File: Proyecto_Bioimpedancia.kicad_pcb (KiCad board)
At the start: 2 copper layers, 99.9 x 99.8 mm, 67 parts, among them J1 Jumper, J2 Jumper, J3 Jumper_Calibration, J4 Jumper, J5 Jumper, J6 Jumper, P1 CONN_01X05, P10 CONN_01X03, P11 CONN_01X02, P12 CONN_01X01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

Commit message: PCB-1_Prototipo_1
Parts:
- removed C14: 10uF, Capacitors_SMD:C_0805_HandSoldering
- removed P17: CONN_01X02, Socket_Strips:Socket_Strip_Straight_1x02_Pitch2.54mm
- added D3: Z_PROTEC, Diodes_THT:D_DO-41_SOD81_P10.16mm_Horizontal, F.Cu at (141.2, 70.6)
- added D4: Z_PROTEC, Diodes_THT:D_DO-41_SOD81_P10.16mm_Horizontal, F.Cu at (136.8, 65.0)
- added R17: 10K, Resistors_SMD:R_0805_HandSoldering, F.Cu at (133.9, 63.6)
- added W6: TEST_1P, Measurement_Points:Measurement_Point_Round-TH_Small, F.Cu at (100.4, 104.7)
- C10: value 1uF -> 0,1uF
- C11: value 1uF -> 10uF
- C13: value 1nF -> 10uF; footprint Capacitors_SMD:C_1206_HandSoldering -> Capacitors_SMD:C_0805_HandSoldering
- P1: value CONN_01X05 -> PROTECCION_MICRO; footprint Socket_Strips:Socket_Strip_Straight_1x05_Pitch2.54mm -> Sockets_MOLEX_KK-System:Socket_MOLEX-KK-RM3-96mm_Lock_3pin_straight
- P10: value CONN_01X03 -> RS-232
- P11: value CONN_01X02 -> SOURCE_2; footprint Socket_Strips:Socket_Strip_Straight_1x02_Pitch2.54mm -> Sockets_MOLEX_KK-System:Socket_MOLEX-KK-RM3-96mm_Lock_2pin_straight
- P12: value CONN_01X01 -> RESET
- P13: value CONN_01X02 -> POWER; footprint Socket_Strips:Socket_Strip_Straight_1x02_Pitch2.54mm -> Sockets_MOLEX_KK-System:Socket_MOLEX-KK-RM3-96mm_Lock_2pin_straight
- P14: value CONN_01X02 -> BIO_OUT1; footprint Socket_Strips:Socket_Strip_Straight_1x02_Pitch2.54mm -> Sockets_MOLEX_KK-System:Socket_MOLEX-KK-RM3-96mm_Lock_2pin_straight
- P15: value CONN_01X01 -> GND_REGULATOR
- P16: value CONN_01X02 -> BIO_OUT2; footprint Socket_Strips:Socket_Strip_Straight_1x02_Pitch2.54mm -> Sockets_MOLEX_KK-System:Socket_MOLEX-KK-RM3-96mm_Lock_2pin_straight
- P2: value CONN_01X08 -> GPIO
- P3: value CONN_01X02 -> SOURCE_3; footprint Socket_Strips:Socket_Strip_Straight_1x02_Pitch2.54mm -> Sockets_MOLEX_KK-System:Socket_MOLEX-KK-RM3-96mm_Lock_2pin_straight
- P4: value CONN_01X04 -> SERIAL_VIRTUAL
- P5: value CONN_01X04 -> ENCODER
- P6: value CONN_01X02 -> I2C_1
- P7: value CONN_01X02 -> I2C_2
- P8: value CONN_01X02 -> SOURCE_1; footprint Socket_Strips:Socket_Strip_Straight_1x02_Pitch2.54mm -> Sockets_MOLEX_KK-System:Socket_MOLEX-KK-RM3-96mm_Lock_2pin_straight
- P9: value CONN_01X04 -> SPI
- R13: value 10K -> 1K
- R14: value 78,7K -> R_PROTEC; footprint Resistors_SMD:R_0805_HandSoldering -> Resistors_ThroughHole:R_Axial_DIN0414_L11.9mm_D4.5mm_P20.32mm_Horizontal
- R15: value 140K -> R_PROTEC; footprint Resistors_SMD:R_0805_HandSoldering -> Resistors_ThroughHole:R_Axial_DIN0414_L11.9mm_D4.5mm_P20.32mm_Horizontal
- R16: value 1K -> 10K
- R2, R3, R5, R6: value 50K -> 20K
- U4: value ADP3334 -> LD1117S50TR; footprint Housings_SOIC:SOIC-8_3.9x4.9mm_Pitch1.27mm -> TO_SOT_Packages_SMD:SOT-223
- moved R15 60.3 mm to (161.6, 60.6), turned to 180 degrees
- moved R14 39.5 mm to (141.2, 65.9)
- moved R16 39.2 mm to (142.6, 73.5), turned to 0 degrees
- moved R13 17.3 mm to (118.1, 103.6)
- moved P4 15.8 mm to (126.1, 48.9)
- moved P1 13.7 mm to (148.8, 52.7), turned to 0 degrees
- moved C13 11.3 mm to (119.9, 88.8), turned to 90 degrees
- moved R12 9.55 mm to (105.6, 101.5)
- moved C10 8.87 mm to (104.3, 94.6), turned to 0 degrees
- moved C11 7.45 mm to (113.2, 95.1), turned to 180 degrees
- moved R10 6.41 mm to (169.3, 88.3), turned to 180 degrees
- moved D1 5.01 mm to (106.6, 107.3)
- moved U4 4.79 mm to (112.0, 101.8), turned to 270 degrees
- moved J4 4.56 mm to (172.4, 85.0)
- moved W5 4.30 mm to (123.7, 98.9)
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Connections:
- BIO1 pad 10: /3V3 -> /5V
- BIO1 pad 11: /3V3 -> /5V
- BIO1 pad 9: /3V3 -> /5V
- C10 pad 1: /V_FUENTE -> /AGND
- C10 pad 2: /AGND -> /V_FUENTE
- C11 pad 1: Net-(C11-Pad1) -> /AGND
- C11 pad 2: /AGND -> Net-(C11-Pad2)
- C12 pad 2: /3V3 -> /5V
- C13 pad 1: Net-(C13-Pad1) -> /5V
- C13 pad 2: Net-(C11-Pad1) -> /AGND
- C2 pad 1: /3V3 -> /5V
- C3 pad 1: /3V3 -> /5V
- C4 pad 1: /3V3 -> /5V
- C7 pad 2: /3V3 -> /5V
- C8 pad 1: /3V3 -> /5V
- C9 pad 1: /3V3 -> /5V
- J6 pad 1: /3V3 -> /5V
- J6 pad 2: Net-(C11-Pad1) -> Net-(C11-Pad2)
- P1 pad 1: /V_FUENTE -> /REG1_1
- P1 pad 2: /REG1_1 -> Net-(P1-Pad2)
- P1 pad 3: /REG1_2 -> Net-(P1-Pad3)
- P10 pad 1: /TXD -> /AGND
- P10 pad 2: /RXD -> /TXD
- P10 pad 3: /AGND -> /RXD
- P11 pad 1: /V_FUENTE -> /5V
- P2 pad 1: /V_FUENTE -> /5V
- P3 pad 1: /V_FUENTE -> /5V
- P4 pad 1: /V_FUENTE -> /5V
- P5 pad 1: /V_FUENTE -> /5V
- P8 pad 1: /V_FUENTE -> /5V
- R1 pad 1: /3V3 -> /5V
- R11 pad 1: /3V3 -> /5V
- R13 pad 1: /AGND -> Net-(C11-Pad2)
- R13 pad 2: /D_REG -> Net-(D2-Pad2)
- R14 pad 1: /AGND -> /REG1_3
- R14 pad 2: Net-(C13-Pad1) -> Net-(P1-Pad2)
- R15 pad 1: Net-(C13-Pad1) -> Net-(P1-Pad3)
- R15 pad 2: Net-(C11-Pad1) -> /REG1_2
- R16 pad 1: Net-(C11-Pad1) -> /REG1_3
- R16 pad 2: Net-(D2-Pad2) -> /AGND
- R2 pad 1: /3V3 -> /5V
- R4 pad 1: /3V3 -> /5V
- R5 pad 1: /3V3 -> /5V
- U1 pad 8: /3V3 -> /5V
- U2 pad 4: /3V3 -> /5V
- U3 pad 1: /TX_V -> /REG1_3
- U3 pad 10: /REG1_2 -> /TX_V
- U3 pad 11: /REG1_3 -> /RX_V
- U3 pad 18: /3V3 -> /5V
- U3 pad 2: /RX_V -> /REG1_2
- U3 pad 20: /3V3 -> /5V
- U3 pad 4: /3V3 -> /5V
- U3 pad 6: /3V3 -> /5V
- U4 pad 2: /D_REG -> Net-(C11-Pad2)
- U4 pad 4: /V_FUENTE -> (no net)
- W5 pad 1: /3V3 -> /5V
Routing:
- net /5V: track 0.00 -> 382.6 mm, vias 0 -> 26
- net /3V3: track 215.0 -> 0.00 mm, vias 17 -> 0
- net /V_FUENTE: track 215.9 -> 29.5 mm, vias 8 -> 0
- net Net-(C11-Pad2): track 0.00 -> 27.9 mm
- net /TX_V: track 46.3 -> 23.8 mm
- net /RX_V: track 43.8 -> 22.3 mm
- net Net-(C11-Pad1): track 20.9 -> 0.00 mm
- net Net-(P1-Pad2): track 0.00 -> 20.8 mm
- net Net-(P1-Pad3): track 0.00 -> 14.3 mm
- net /REG1_3: track 20.8 -> 35.0 mm
- net Net-(C13-Pad1): track 14.0 -> 0.00 mm
- net /RESET: track 78.4 -> 89.0 mm
- net /REG1_1: track 23.2 -> 33.2 mm
- net /RXD: track 69.7 -> 79.1 mm
- net Net-(J4-Pad2): track 19.3 -> 11.6 mm
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- added copper zone on F.Cu, net /5V
- removed copper zone on F.Cu, net /3V3

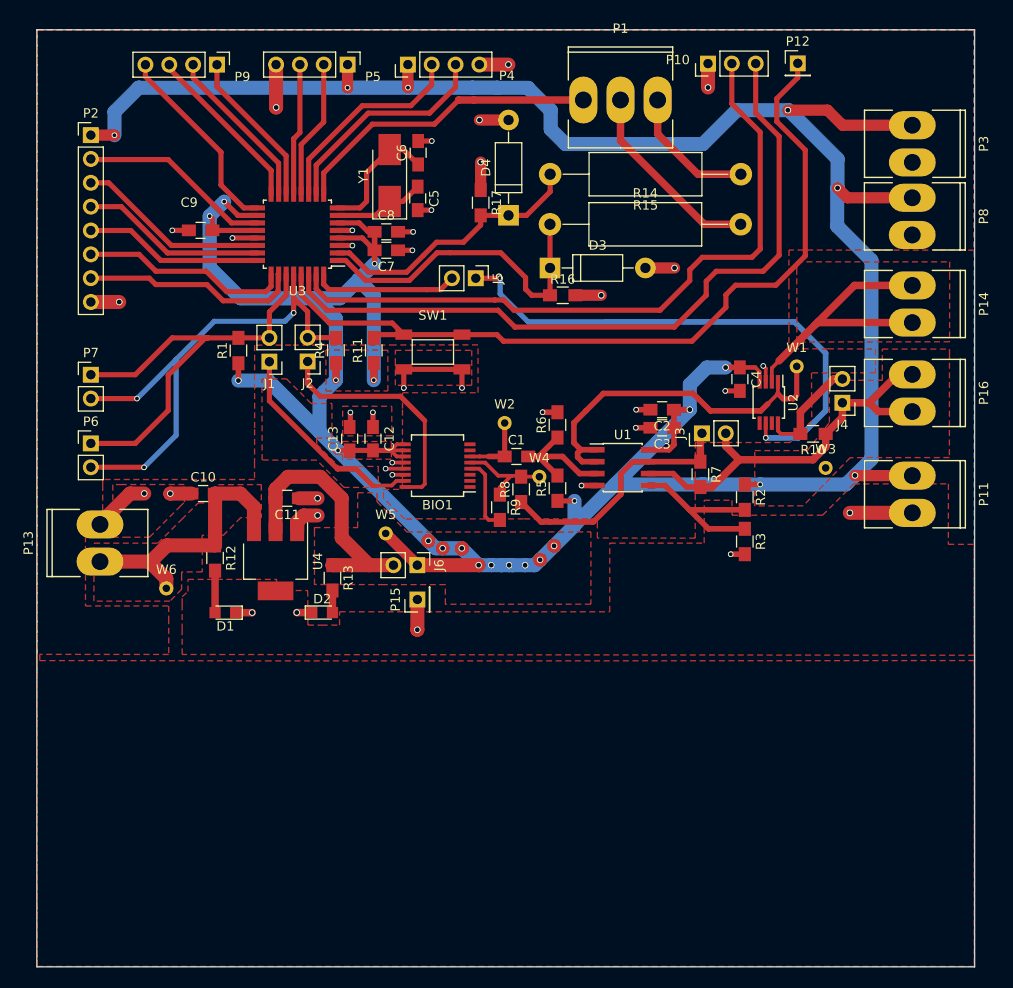
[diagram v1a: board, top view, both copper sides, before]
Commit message: Cambio de limites de la PCB
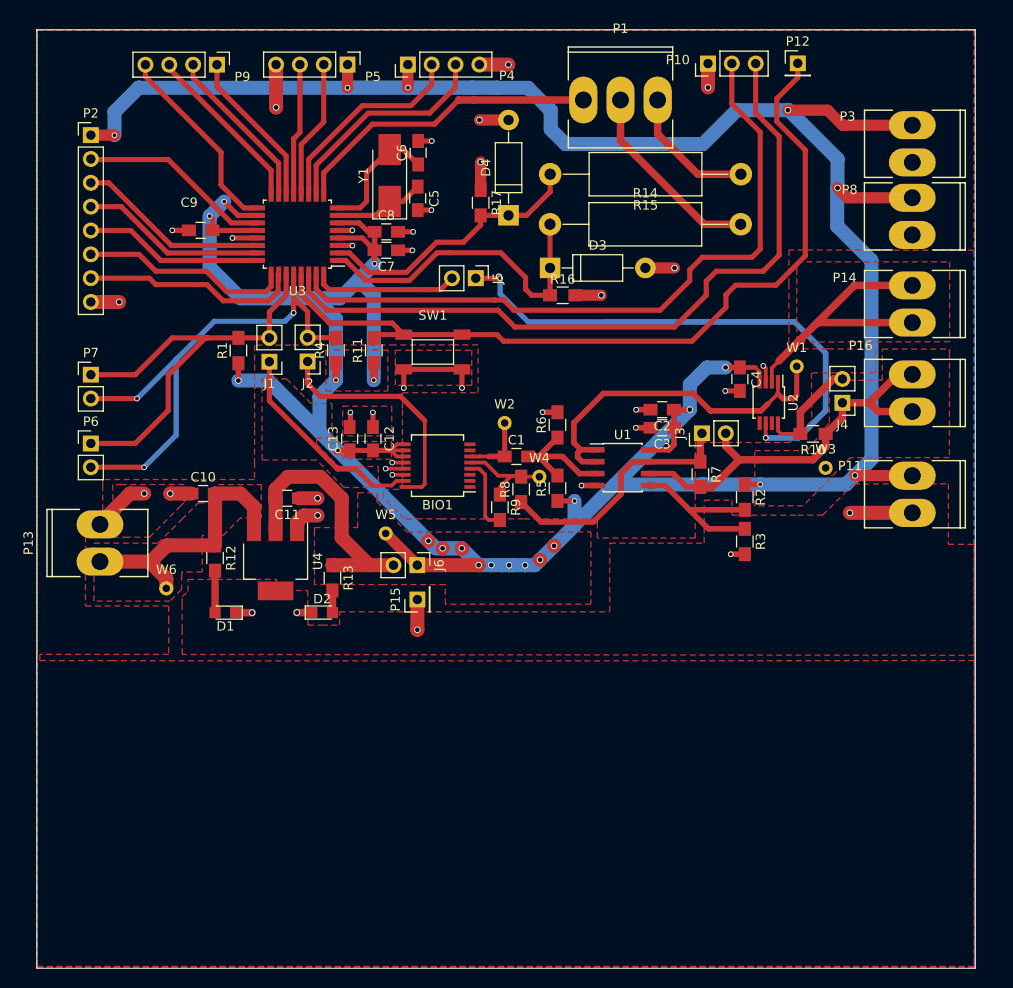
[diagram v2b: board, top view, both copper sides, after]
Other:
- board size 99.9 x 99.8 mm -> 100 x 100 mm
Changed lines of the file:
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@@
     (descr "Socket, MOLEX, KK, RM 3.96mm, Lock, 2pin, straight,")
     (tags "Socket, MOLEX, KK, RM 3.96mm, Lock, 2pin, straight,")
-    (fp_text reference P3 (at 0 -7.62 270) (layer F.SilkS)
+    (fp_text reference P3 (at -2.91846 6.91134 360) (layer F.SilkS)
       (effects (font (size 1 1) (thickness 0.15)))
     )
@@
     (descr "Socket, MOLEX, KK, RM 3.96mm, Lock, 2pin, straight,")
     (tags "Socket, MOLEX, KK, RM 3.96mm, Lock, 2pin, straight,")
-    (fp_text reference P8 (at 0 -7.62 270) (layer F.SilkS)
+    (fp_text reference P8 (at -2.83972 6.67512 360) (layer F.SilkS)
       (effects (font (size 1 1) (thickness 0.15)))
     )
@@
     (descr "Socket, MOLEX, KK, RM 3.96mm, Lock, 2pin, straight,")
     (tags "Socket, MOLEX, KK, RM 3.96mm, Lock, 2pin, straight,")
-    (fp_text reference P11 (at 0 -7.62 270) (layer F.SilkS)
+    (fp_text reference P11 (at -3.01752 6.64464 360) (layer F.SilkS)
       (effects (font (size 1 1) (thickness 0.15)))
     )
@@
     (descr "Socket, MOLEX, KK, RM 3.96mm, Lock, 2pin, straight,")
     (tags "Socket, MOLEX, KK, RM 3.96mm, Lock, 2pin, straight,")
-    (fp_text reference P14 (at 0 -7.62 270) (layer F.SilkS)
+    (fp_text reference P14 (at -2.80416 7.21868 360) (layer F.SilkS)
       (effects (font (size 1 1) (thickness 0.15)))
     )
@@
     (descr "Socket, MOLEX, KK, RM 3.96mm, Lock, 2pin, straight,")
     (tags "Socket, MOLEX, KK, RM 3.96mm, Lock, 2pin, straight,")
-    (fp_text reference P16 (at 0 -7.62 270) (layer F.SilkS)
+    (fp_text reference P16 (at -5.04444 5.50164 360) (layer F.SilkS)
       (effects (font (size 1 1) (thickness 0.15)))
     )
@@
     )
   )
-  (gr_line (start 86.5632 145.0594) (end 86.5632 45.212) (angle 90) (layer Edge.Cuts) (width 0.1))
+  (gr_line (start 86.5632 145.212) (end 86.5632 45.212) (angle 90) (layer Edge.Cuts) (width 0.1))
   (gr_line (start 87.46998 100.84816) (end 87.51824 100.84816) (angle 90) (layer F.Mask) (width 0.2))
   (gr_line (start 185.674 103.69296) (end 185.66384 103.69296) (angle 90) (layer B.CrtYd) (width 0.2))
-  (gr_line (start 86.5632 145.0594) (end 186.4868 145.0594) (angle 90) (layer Edge.Cuts) (width 0.1))
-  (gr_line (start 186.4868 145.0594) (end 186.4868 45.212) (angle 90) (layer Edge.Cuts) (width 0.1))
-  (gr_line (start 86.5632 45.212) (end 186.4868 45.212) (angle 90) (layer Edge.Cuts) (width 0.1))
+  (gr_line (start 86.5632 145.212) (end 186.5632 145.212) (angle 90) (layer Edge.Cuts) (width 0.1))
+  (gr_line (start 186.5632 145.212) (end 186.5632 45.212) (angle 90) (layer Edge.Cuts) (width 0.1))
+  (gr_line (start 86.5632 45.212) (end 186.5632 45.212) (angle 90) (layer Edge.Cuts) (width 0.1))
   (segment (start 132.70552 91.97836) (end 133.69786 91.97836) (width 0.4) (layer F.Cu) (net 1))
   (segment (start 134.70508 97.44328) (end 135.90016 97.44328) (width 0.4) (layer F.Cu) (net 1))

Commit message: Cambio de nombre regleta SD_LAPIZ
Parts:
- P1: value PROTECCION_MICRO -> SD_LAPIZ
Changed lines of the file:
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@@
     (links 150)
     (no_connects 0)
-    (area 84.44666 43.84984 188.54478 145.109401)
+    (area 86.513199 45.161999 186.613201 145.262001)
     (thickness 1.6)
     (drawings 6)
@@
       (effects (font (size 1 1) (thickness 0.15)))
     )
-    (fp_text value PROTECCION_MICRO (at -0.1524 -6.3246) (layer F.Fab)
-      (effects (font (size 1 1) (thickness 0.15)))
-    )
+    (fp_text value SD_LAPIZ (at -0.1524 -6.3246) (layer F.Fab)
+      (effects (font (size 1 1) (thickness 0.15)))
+    )

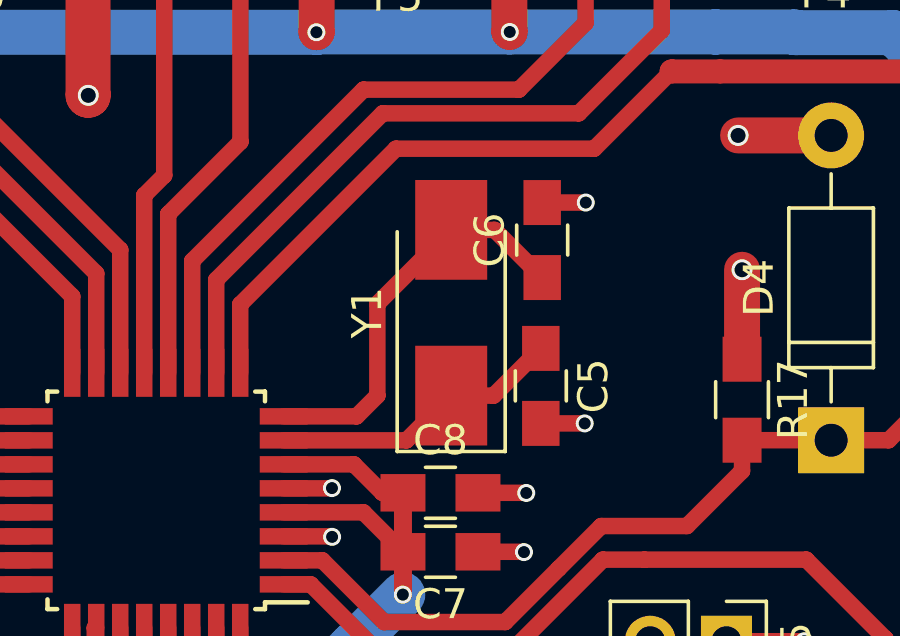
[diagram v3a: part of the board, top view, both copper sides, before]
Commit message: Cambio de clock
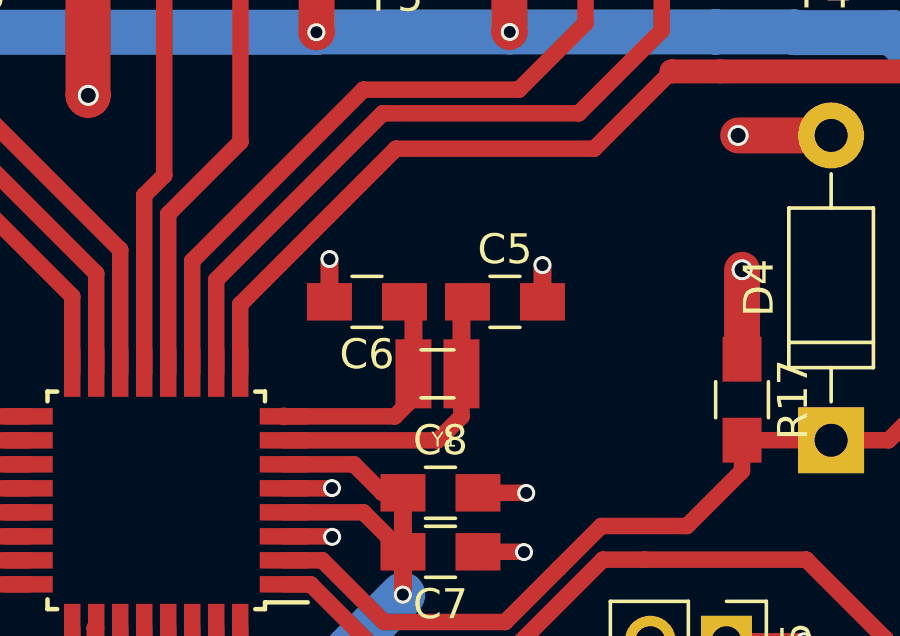
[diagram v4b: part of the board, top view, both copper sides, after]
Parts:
- C5, C6: value 18pF -> 8pF
- Y1: value AMB3_16M -> XRCHA_16M; footprint Crystals:Crystal_SMD_Abracon_ABM3-2pin_5.0x3.2mm_HandSoldering -> Huellas:Crystal_SMD_XRCHA_Murata_Serie_W2,5mm_L2,0mm
- moved C6 6.19 mm to (121.3, 60.4), turned to 180 degrees
- moved C5 3.05 mm to (126.0, 60.4), turned to 0 degrees
- moved Y1 2.09 mm to (123.7, 62.8), turned to 180 degrees
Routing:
- net /CLK2: track 13.6 -> 8.42 mm

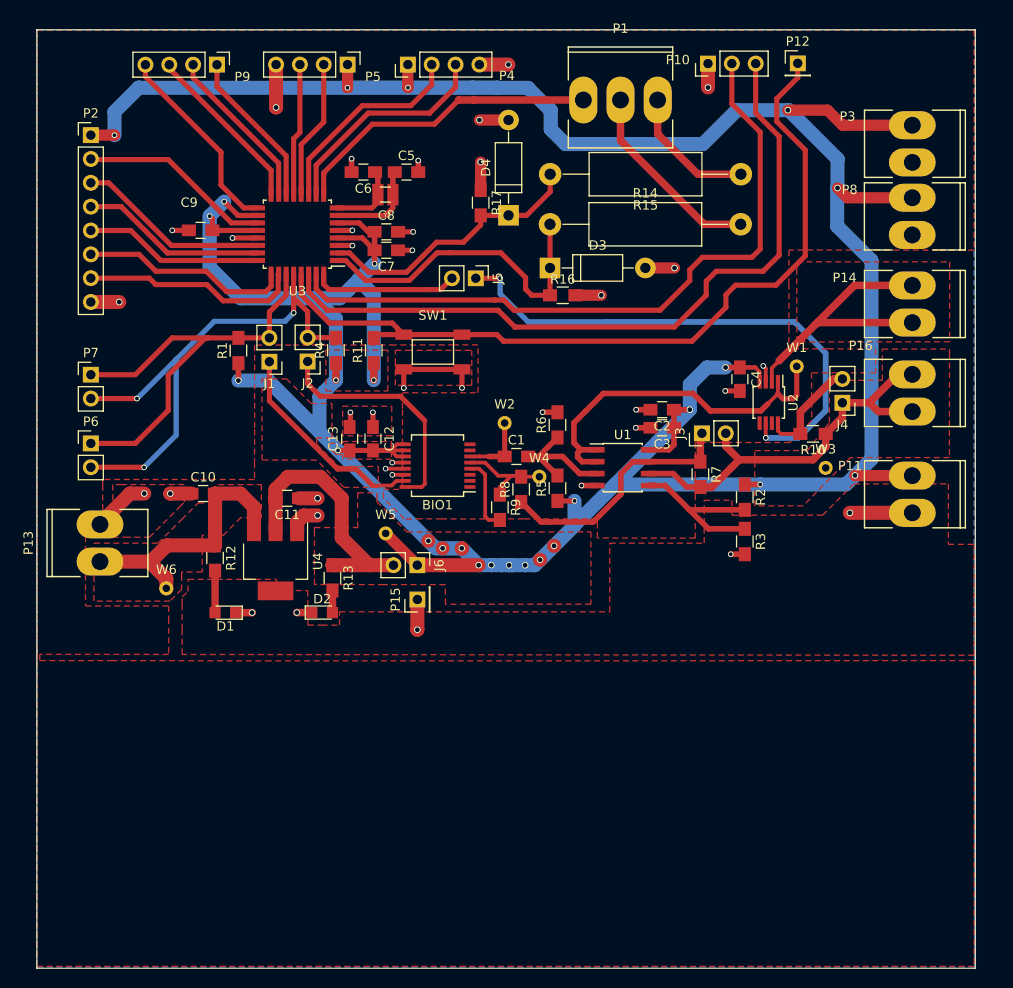
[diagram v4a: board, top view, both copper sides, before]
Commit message: Correcciones PCB BIO
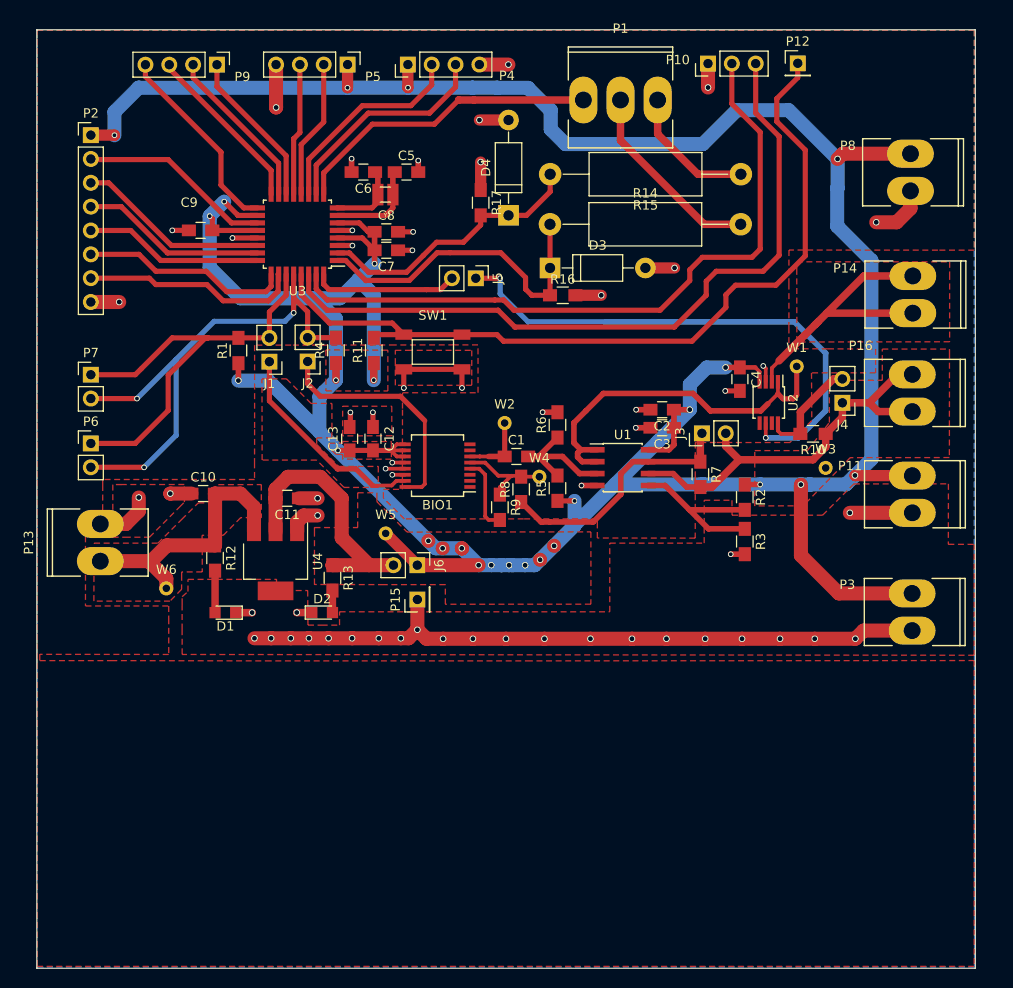
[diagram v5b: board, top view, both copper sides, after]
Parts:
- moved P3 49.9 mm to (179.8, 107.2)
- moved P8 4.70 mm to (179.7, 60.4)
- moved P14 1.01 mm to (179.9, 73.4)
- moved P13 0.06 mm to (93.3, 99.8)
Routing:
- net /AGND: track 95.2 -> 172.6 mm, vias 38 -> 59
- net /5V: track 382.6 -> 389.5 mm
- removed copper zone on F.Cu, net (none)
